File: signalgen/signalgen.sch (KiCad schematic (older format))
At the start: 32 parts, among them CON1 USB-MINI-B, J1 SWDCONN, U1 OSC-16MHZ, U2 ADP1715-3.3, U5 OSC-50MHZ, U6 LTC1983-5, U7 MCP4542

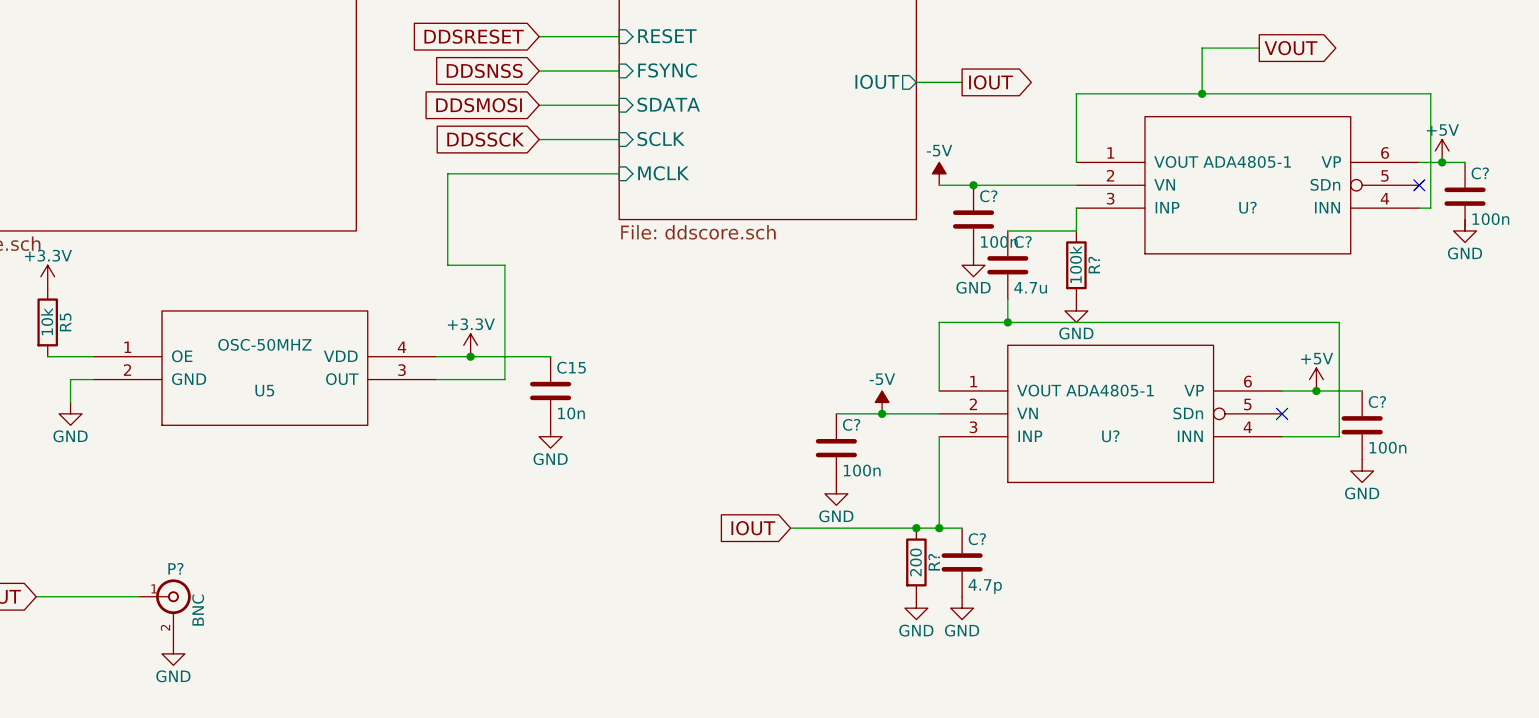
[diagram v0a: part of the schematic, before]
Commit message: First layout of DDS signal generator.
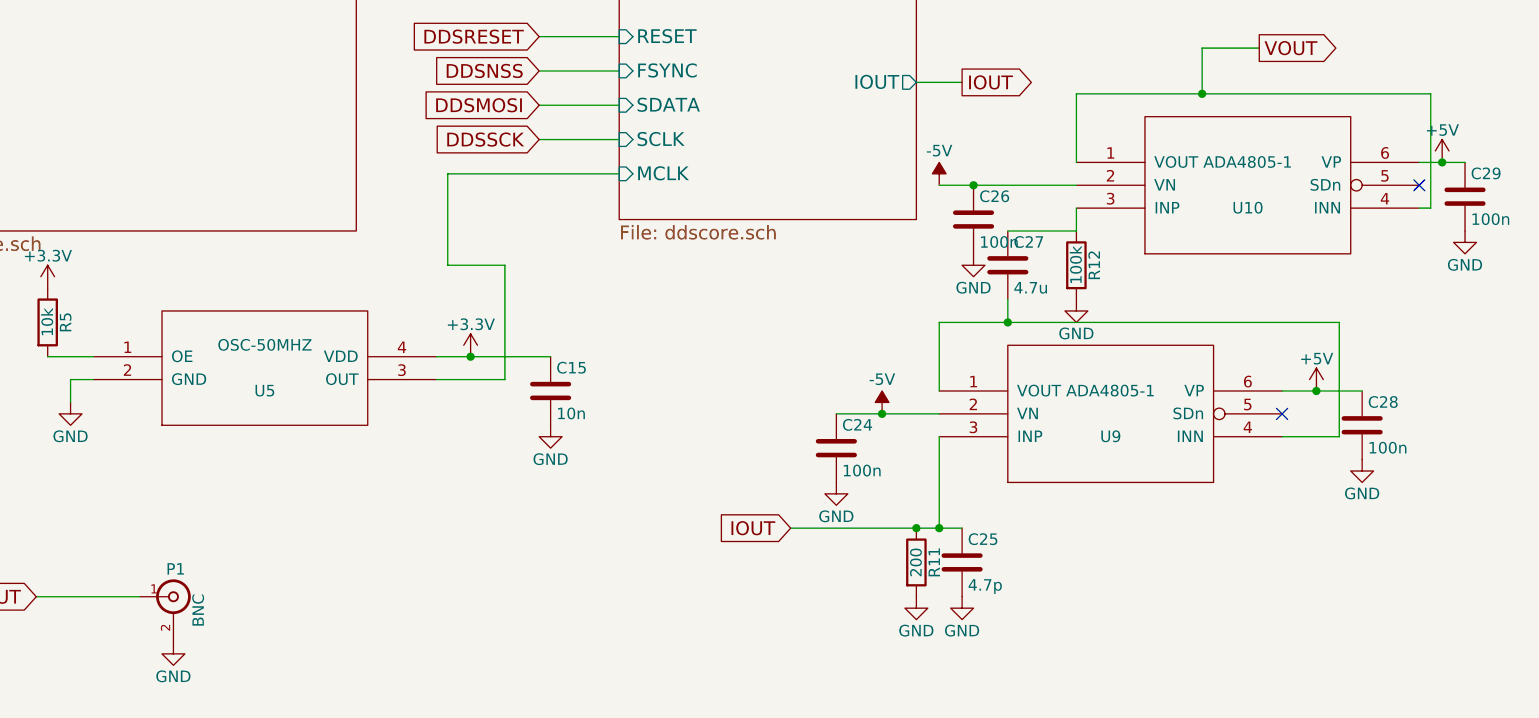
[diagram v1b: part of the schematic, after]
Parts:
- C24, C26, C28, C29: renamed from C?; footprint (none) -> Capacitors_SMD:C_0402
- C25, C27: renamed from C?; footprint (none) -> Capacitors_SMD:C_0603
- P1: renamed from P?; footprint (none) -> w_conn_rf:sma_straight_32k101-400l5
- R11, R12: renamed from R?; footprint (none) -> Resistors_SMD:R_0402
- U10, U9: renamed from U?; footprint MODULE -> Housings_SOT-23_SOT-143_TSOT-6:SC-70-6
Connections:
- net GND: now also C29.2
